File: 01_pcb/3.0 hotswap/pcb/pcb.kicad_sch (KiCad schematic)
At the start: 128 parts, among them J1 TYPE-C-31-M12_13, J2 AVR-ISP-6_mod, J3 4PIN, J5 Conn_01x08, SW1 SW_PUSH, U1 ATmega32U4-M, U2 PRTR5V0U2X, Y1 16MHz

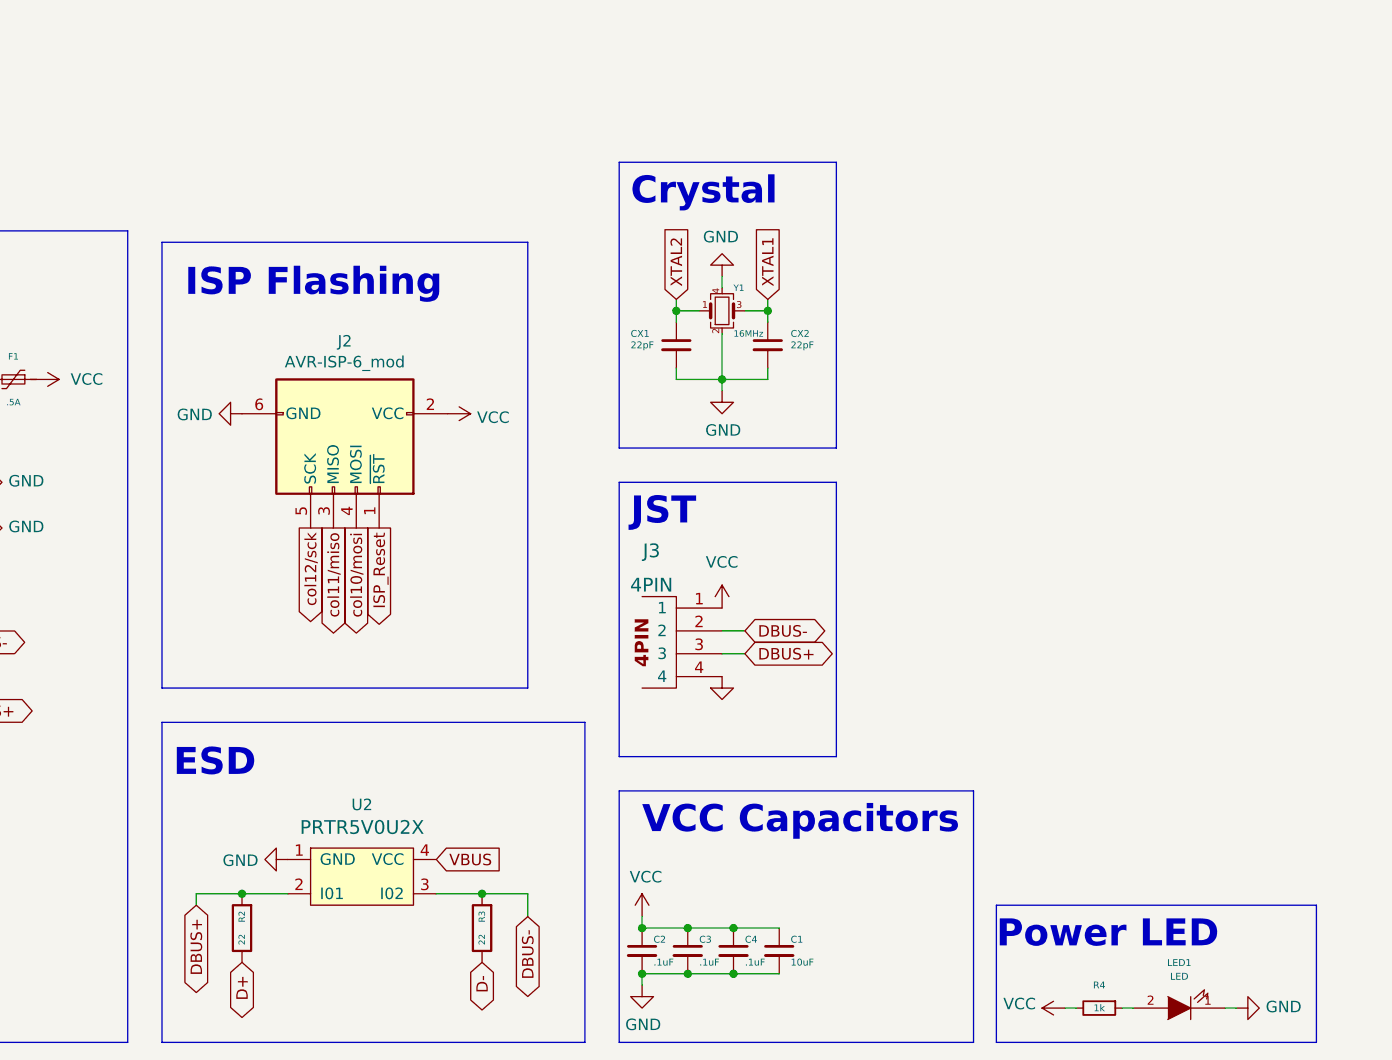
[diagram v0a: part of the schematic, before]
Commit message: add stitching vias
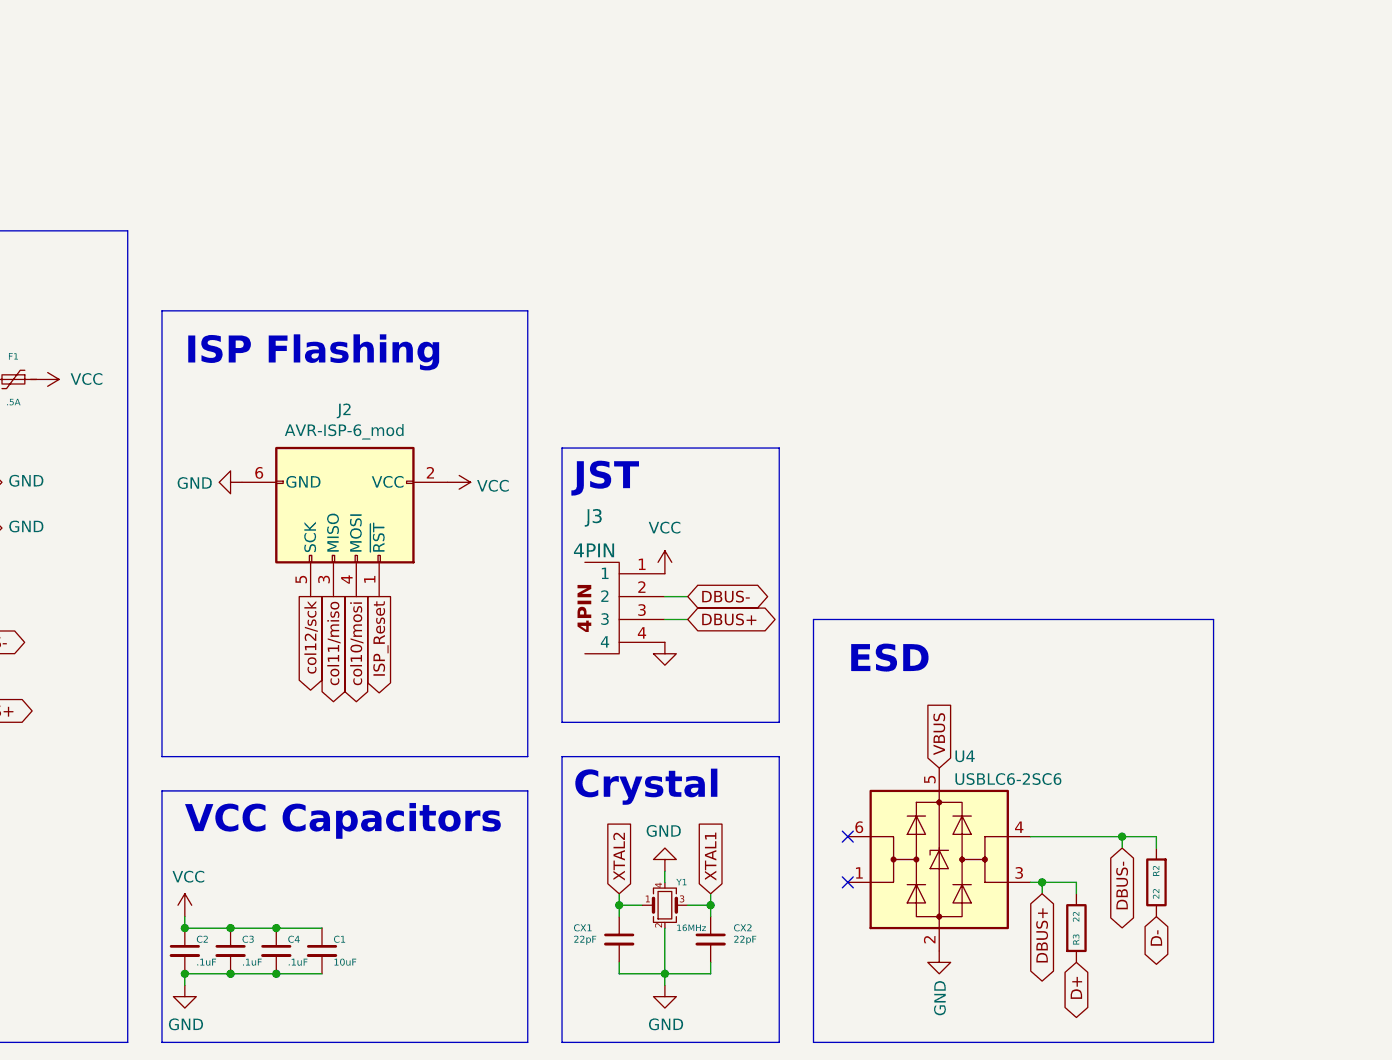
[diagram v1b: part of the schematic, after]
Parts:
- removed LED1: LED, LED_SMD:LED_0805_2012Metric_Pad1.15x1.40mm_HandSolder, symbol pcb-rescue:LED-keyboard_parts-Ori-rescue-lucy-rescue
- removed R4: 1k, Resistor_SMD:R_0603_1608Metric, symbol Device:R_Small
- removed U2: PRTR5V0U2X, Package_TO_SOT_SMD:SOT-143, symbol keyboard_parts:PRTR5V0U2X
- added U4: USBLC6-2SC6, Package_TO_SOT_SMD:SOT-23-6, symbol Power_Protection:USBLC6-2SC6
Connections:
- net D+: now also R3.2; no longer R2.1
- net D-: now also R2.1; no longer R3.1
- net DBUS+: now also R3.1, U4.3 (I/O2); no longer R2.2
- net DBUS-: now also R2.2, U4.4 (I/O2); no longer R3.2
- net GND: now also U4.2 (GND)
- net VBUS: now also U4.5 (VBUS)
- no-connect marks 3 -> 5
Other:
- note removed: "Power LED"
- moved on the sheet: C1, C2, C3, C4, CX1, CX2, J2, J3, R2, R3, Y1

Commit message: replaced SRV05-4 footprint
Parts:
- U4: footprint Package_TO_SOT_SMD:SOT-23-6 -> marbastlib-various:SOT-23-6-routable
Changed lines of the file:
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@@
       (effects (font (size 1.27 1.27)) (justify left))
     )
-    (property "Footprint" "Package_TO_SOT_SMD:SOT-23-6" (at 252.73 267.97 0)
+    (property "Footprint" "marbastlib-various:SOT-23-6-routable" (at 252.73 267.97 0)
       (effects (font (size 1.27 1.27)) hide)
     )
